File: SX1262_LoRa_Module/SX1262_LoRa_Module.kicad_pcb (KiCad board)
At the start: 4 copper layers, 45 x 27.5 mm, 36 parts, among them Q1 32.0Mhz, U1 SX1262IMLTRT, U2 PE4259

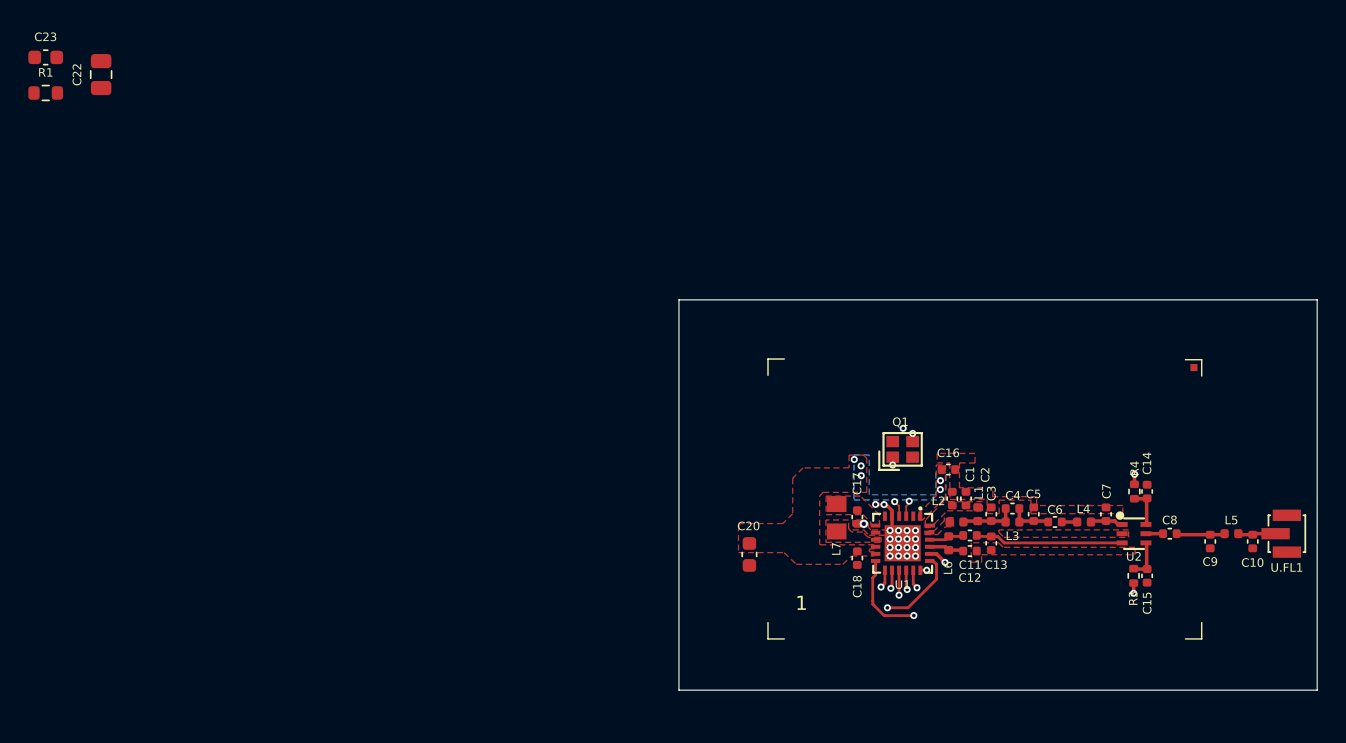
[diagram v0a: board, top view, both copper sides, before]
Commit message: -pcb
-done pcb routing
-including castellated pads
-warnings and error is due to tight placement of the components for the filter and tuning
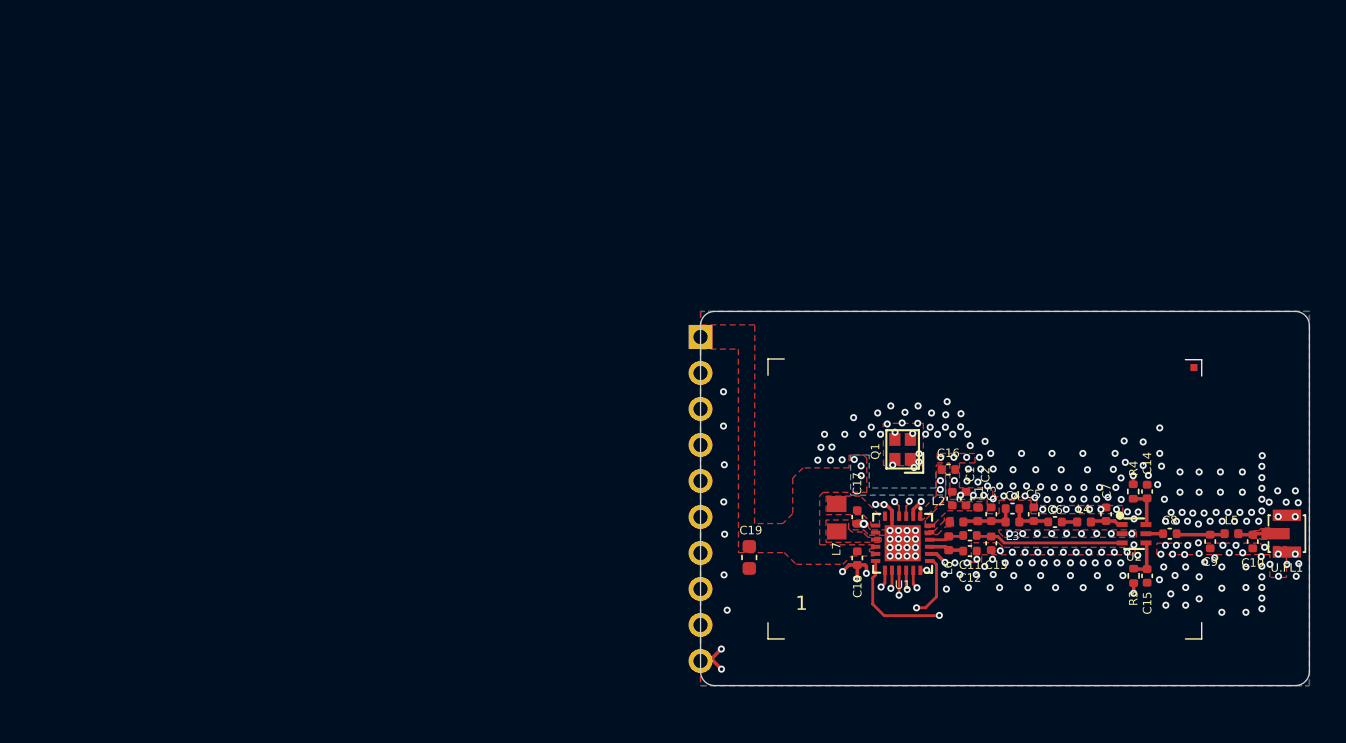
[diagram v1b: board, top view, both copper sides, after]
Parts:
- removed C20: 1uF, Capacitor_SMD:C_0603_1608Metric
- removed C22: 10uF, Capacitor_SMD:C_0805_2012Metric
- removed C23: 100nF, Capacitor_SMD:C_0603_1608Metric
- removed R1: 0R, Resistor_SMD:R_0603_1608Metric
- added C19: 1uF, Capacitor_SMD:C_0603_1608Metric, F.Cu at (140.4, 106.7)
- added J1: Conn_01x10_Pin, Connector_PinHeader_2.54mm:PinHeader_1x10_P2.54mm_Vertical, F.Cu at (136.9, 91.1)
- moved R4 0.08 mm to (167.5, 102.0)
- turned Q1 to 90 degrees
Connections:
- Shield pad 1: (no net) -> GND
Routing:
- net /ANT_SW: track 0.72 -> 41.3 mm
- net /DIO1: track 1.29 -> 24.1 mm
- net /BUSY: track 1.31 -> 22.8 mm
- net /NRESET: track 1.76 -> 22.1 mm
- net /MISO: track 1.39 -> 21.0 mm
- net /SCK: track 0.45 -> 19.6 mm
- net /MOSI: track 1.34 -> 19.5 mm
- net /DIO2: track 7.09 -> 23.6 mm
- net /NSS: track 5.93 -> 21.1 mm
- net GND: track 13.1 -> 21.4 mm, vias 21 -> 265
- net /XTB: vias 2 -> 5
- net /XTA: vias 2 -> 3
- added copper zone on B.Cu, net GND
- added copper zone on In1.Cu, net GND
- added copper zone on In2.Cu, net GND
- added copper zone on F.Cu, net Net-(C10-Pad2)
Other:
- board size 45 x 27.5 mm -> 43 x 26.4 mm

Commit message: -reupload
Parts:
- turned Q1 to 0 degrees
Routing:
- net GND: vias 265 -> 269
- net /XTB: vias 5 -> 2
- net /XTA: vias 3 -> 2
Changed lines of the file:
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@@
 	(footprint "Lora_Footprint_Library:CRYSTAL-SMD_4P-L2.0-W1.6-BL"
 		(layer "F.Cu")
-		(at 151.2011 99.0536 90)
+		(at 151.2011 99.0536)
 		(property "Reference" "Q1"
-			(at -0.15 -1.926 90)
+			(at -0.15 -1.926 0)
 			(layer "F.SilkS")
 			(effects
@@
 		)
 		(property "Value" "32.0Mhz"
-			(at -0.15 2.226 90)
+			(at -0.15 2.226 0)
 			(layer "F.Fab")
 			(effects
@@
 		)
 		(property "Datasheet" ""
-			(at 0 0 90)
+			(at 0 0 0)
 			(layer "F.Fab")
 			(hide yes)
@@
 		)
 		(property "Description" "Four pin crystal, GND on pins 2 and 4"
-			(at 0 0 90)
+			(at 0 0 0)
 			(layer "F.Fab")
 			(hide yes)
@@
 		)
 		(property "LCSC" "C1986260"
-			(at 0 0 90)
+			(at 0 0 0)
 			(unlocked yes)
 			(layer "F.Fab")
@@
 		(sheetfile "SX1262_LoRa_Module.kicad_sch")
 		(fp_line
-			(start 1.35 -1.15)
-			(end 1.35 1.15)
+			(start -1.65 0.15)
+			(end -1.65 1.45)
 			(stroke
 				(width 0.152)
@@
 		)
 		(fp_line
-			(start -1.35 -1.15)
-			(end 1.35 -1.15)
+			(start -1.65 1.45)
+			(end -0.25 1.45)
 			(stroke
 				(width 0.152)
@@
 		)
 		(fp_line
-			(start -1.65 0.15)
-			(end -1.65 1.45)
+			(start -1.35 -1.15)
+			(end 1.35 -1.15)
 			(stroke
 				(width 0.152)
@@
 		)
 		(fp_line
-			(start 1.35 1.15)
-			(end -1.35 1.15)
+			(start -1.35 1.15)
+			(end -1.35 -1.15)
 			(stroke
 				(width 0.152)
@@
 		)
 		(fp_line
-			(start -1.35 1.15)
-			(end -1.35 -1.15)
+			(start 1.35 -1.15)
+			(end 1.35 1.15)
 			(stroke
 				(width 0.152)
@@
 		)
 		(fp_line
-			(start -1.65 1.45)
-			(end -0.25 1.45)
+			(start 1.35 1.15)
+			(end -1.35 1.15)
 			(stroke
 				(width 0.152)
@@
 		(fp_poly
 			(pts
-				(xy 0.95 -0.75) (xy 0.95 -0.275) (xy 0.375 -0.275) (xy 0.375 -0.75)
+				(xy -0.95 -0.275) (xy -0.95 -0.75) (xy -0.375 -0.75) (xy -0.375 -0.275)
 			)
 			(stroke
@@
 		(fp_poly
 			(pts
-				(xy -0.95 -0.275) (xy -0.95 -0.75) (xy -0.375 -0.75) (xy -0.375 -0.275)
+				(xy -0.95 0.75) (xy -0.95 0.275) (xy -0.375 0.275) (xy -0.375 0.75)
 			)
 			(stroke
@@
 		(fp_poly
 			(pts
-				(xy 0.95 0.275) (xy 0.95 0.75) (xy 0.375 0.75) (xy 0.375 0.275)
+				(xy 0.95 -0.75) (xy 0.95 -0.275) (xy 0.375 -0.275) (xy 0.375 -0.75)
 			)
 			(stroke
@@
 		(fp_poly
 			(pts
-				(xy -0.95 0.75) (xy -0.95 0.275) (xy -0.375 0.275) (xy -0.375 0.75)
+				(xy 0.95 0.275) (xy 0.95 0.75) (xy 0.375 0.75) (xy 0.375 0.275)
 			)
 			(stroke
@@
 		)
 		(fp_line
-			(start 1 -0.8)
-			(end 1 0.8)
+			(start -1 -0.8)
+			(end 1 -0.8)
 			(stroke
 				(width 0.051)
@@
 		)
 		(fp_line
-			(start -1 -0.8)
-			(end 1 -0.8)
+			(start -1 0.8)
+			(end -1 -0.8)
 			(stroke
 				(width 0.051)
@@
 		)
 		(fp_line
-			(start 1 0.8)
-			(end -1 0.8)
+			(start 1 -0.8)
+			(end 1 0.8)
 			(stroke
 				(width 0.051)
@@
 		)
 		(fp_line
-			(start -1 0.8)
-			(end -1 -0.8)
+			(start 1 0.8)
+			(end -1 0.8)
 			(stroke
 				(width 0.051)
@@
 		)
 		(pad "1" smd rect
-			(at -0.7 0.55 90)
+			(at -0.7 0.55)
 			(size 0.9 0.8)
 			(layers "F.Cu" "F.Mask" "F.Paste")
@@
 		)
 		(pad "2" smd rect
-			(at 0.7 0.55 90)
+			(at 0.7 0.55)
 			(size 0.9 0.8)
 			(layers "F.Cu" "F.Mask" "F.Paste")
@@
 		)
 		(pad "3" smd rect
-			(at 0.7 -0.55 90)
+			(at 0.7 -0.55)
 			(size 0.9 0.8)
 			(layers "F.Cu" "F.Mask" "F.Paste")
@@
 		)
 		(pad "4" smd rect
-			(at -0.7 -0.55 90)
+			(at -0.7 -0.55)
 			(size 0.9 0.8)
 			(layers "F.Cu" "F.Mask" "F.Paste")
@@
 	)
 	(via
+		(at 152.01 100.34)
+		(size 0.5)
+		(drill 0.25)
+		(layers "F.Cu" "B.Cu")
+		(free yes)
+		(net 2)
+	)
+	(via
 		(at 151.51 105.98)
 		(size 0.5)
@@
 	)
 	(via
+		(at 150.665 97.84)
+		(size 0.5)
+		(drill 0.25)
+		(layers "F.Cu" "B.Cu")
+		(free yes)
+		(net 2)
+	)
+	(via
 		(at 145.69 97.99)
 		(size 0.5)
@@
 	)
 	(via
+		(at 152.35 99.93)
+		(size 0.5)
+		(drill 0.25)
+		(layers "F.Cu" "B.Cu")
+		(net 2)
+	)
+	(via
 		(at 156.915 102.29)
 		(size 0.5)
@@
 	)
 	(via
+		(at 152.36 99.36)
+		(size 0.5)
+		(drill 0.25)
+		(layers "F.Cu" "B.Cu")
+		(net 2)
+	)
+	(via
 		(at 169.34 99.34)
 		(size 0.5)
@@
 	)
 	(segment
-		(start 151.9011 97.9389)
-		(end 151.91 97.93)
+		(start 151.9011 98.5036)
+		(end 151.9011 97.9389)
 		(width 0.127)
 		(layer "F.Cu")
@@
 	)
 	(segment
-		(start 151.9011 98.5036)
-		(end 151.9011 97.9389)
+		(start 151.9011 97.9389)
+		(end 151.91 97.93)
 		(width 0.127)
 		(layer "F.Cu")
@@
 	)
 	(via
-		(at 150.665 97.84)
-		(size 0.5)
-		(drill 0.25)
-		(layers "F.Cu" "B.Cu")
-		(net 19)
-	)
-	(via
 		(at 151.6635 102.71)
 		(size 0.5)
@@
 	)
 	(segment
-		(start 150.5011 100.1589)
-		(end 150.5 100.16)
+		(start 150.5 99.6047)
+		(end 150.5011 99.6036)
 		(width 0.127)
 		(layer "F.Cu")
@@
 	)
 	(segment
-		(start 150.5011 99.6036)
-		(end 150.5011 100.1589)
+		(start 150.636502 102.742228)
+		(end 150.9511 103.056826)
 		(width 0.127)
 		(layer "F.Cu")
@@
 	)
 	(segment
-		(start 150.636502 102.742228)
-		(end 150.9511 103.056826)
+		(start 150.5 100.16)
+		(end 150.5 99.6047)
 		(width 0.127)
 		(layer "F.Cu")
@@
 	)
 	(via
-		(at 152.01 100.34)
-		(size 0.5)
-		(drill 0.25)
-		(layers "F.Cu" "B.Cu")
-		(net 20)
-	)
-	(via
 		(at 150.6365 102.742228)
 		(size 0.5)
@@
 	)
 	(via
-		(at 152.35 99.93)
-		(size 0.5)
-		(drill 0.25)
-		(layers "F.Cu" "B.Cu")
-		(net 20)
-	)
-	(via
 		(at 150.5 100.16)
 		(size 0.5)
 		(drill 0.25)
-		(layers "F.Cu" "B.Cu")
-		(net 20)
-	)
-	(via
-		(at 152.36 99.36)
-		(size 0.5)
-		(drill 0.25)

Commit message: -added side castellation
-added side castellation
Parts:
- added J2: Conn_01x10_Pin, Connector_PinHeader_2.54mm:PinHeader_1x10_P2.54mm_Vertical, F.Cu at (143.0, 89.3)
- added J3: Conn_01x10_Pin, Connector_PinHeader_2.54mm:PinHeader_1x10_P2.54mm_Vertical, F.Cu at (143.0, 115.7)
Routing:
- net /ANT_SW: track 41.3 -> 40.6 mm

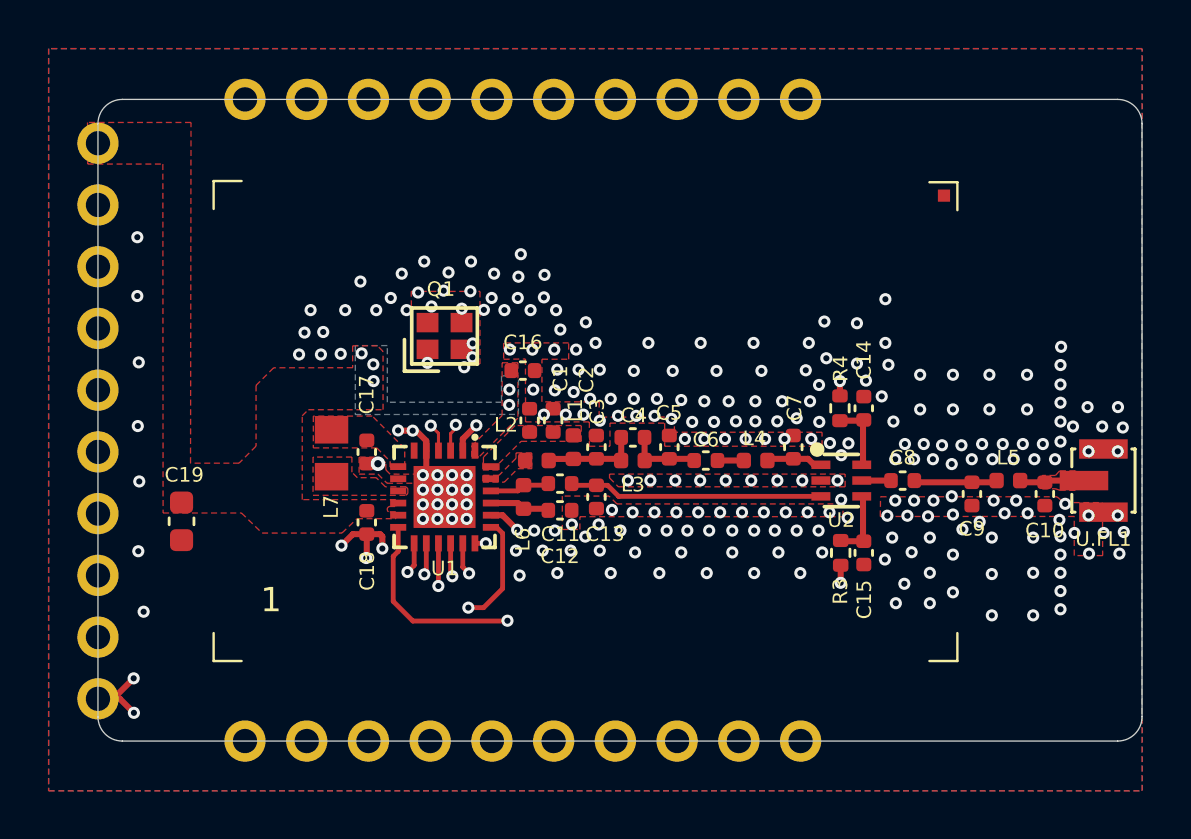
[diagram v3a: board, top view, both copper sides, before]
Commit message: -update bom
-updated bom based on the evm
-put booklet list for the inductor
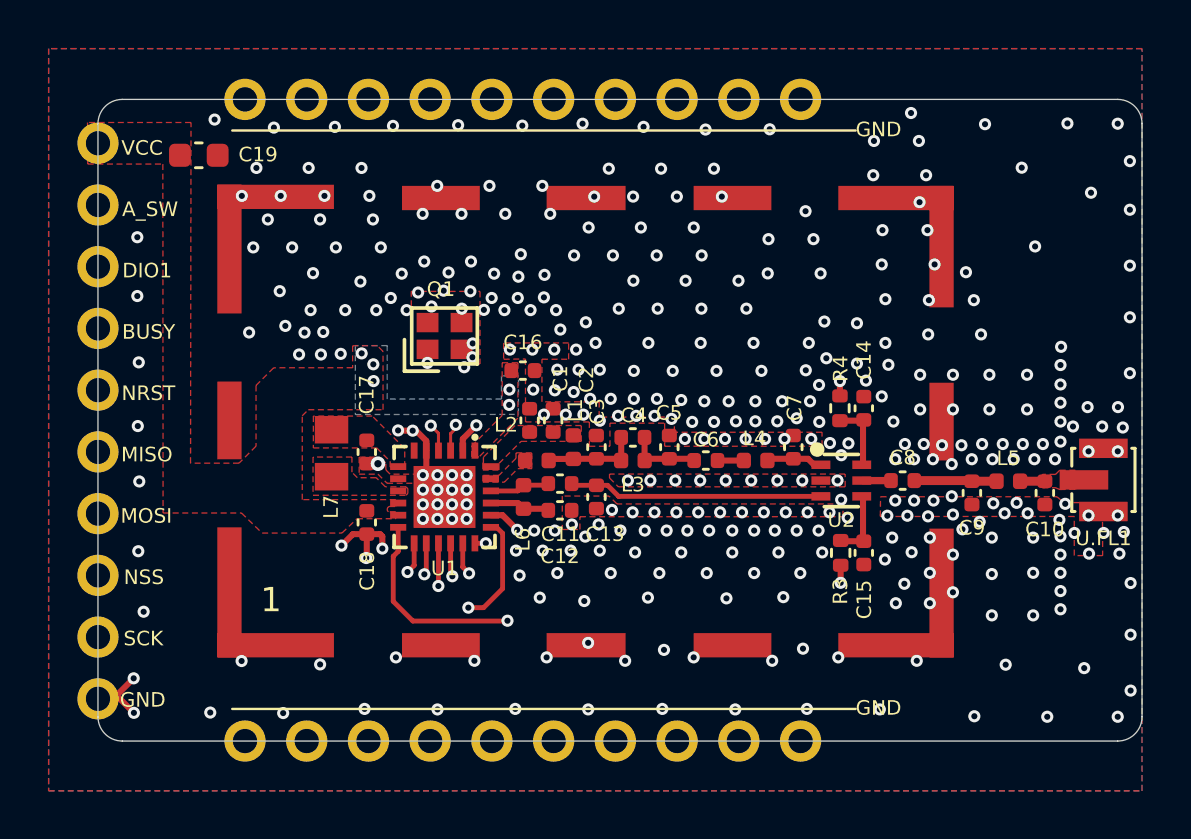
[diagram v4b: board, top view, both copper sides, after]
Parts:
- moved C19 15.1 mm to (141.1, 91.6), turned to 0 degrees
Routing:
- net Net-(C10-Pad2): track 2.68 -> 1.09 mm
- net GND: vias 269 -> 392
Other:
- board text added: "A_SW"
- board text added: "BUSY"
- board text added: "DIO1"
- board text added: "GND"
- board text added: "MISO"
- board text added: "MOSI"
- board text added: "NRST"
- board text added: "NSS"
- board text added: "SCK"
- board text added: "VCC"
